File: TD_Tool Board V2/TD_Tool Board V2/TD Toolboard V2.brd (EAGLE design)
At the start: 54.2 x 49 mm, 140 parts, among them J3 JST-MICROFIT, M1 NMOSFET_WSD3066DN33, M2 CJ3400, M3 CJ3400, M4 CJ3400, P1 TPS54202_BUCKCONV, P2 3.3V, U1 RP2040, U2 W25Q128, U3 SN65HVD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

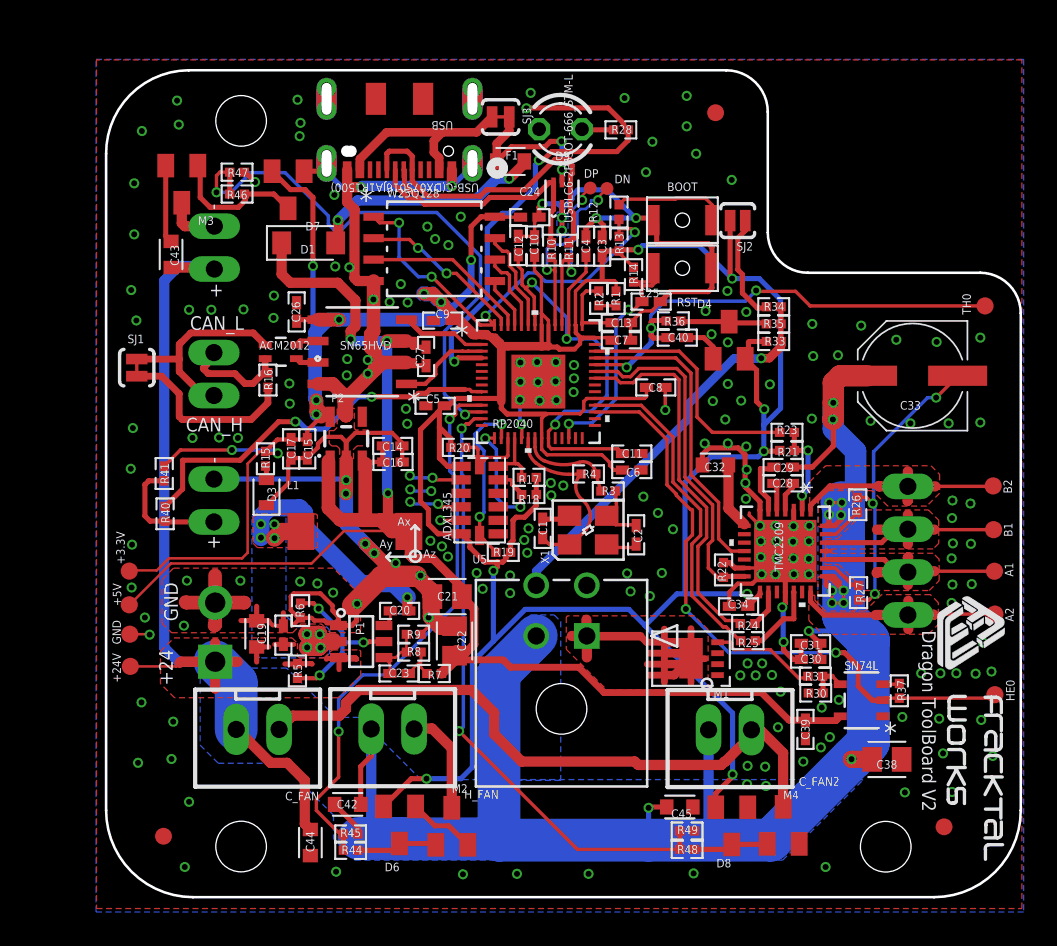
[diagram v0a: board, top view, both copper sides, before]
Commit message: minor changes in connector logic
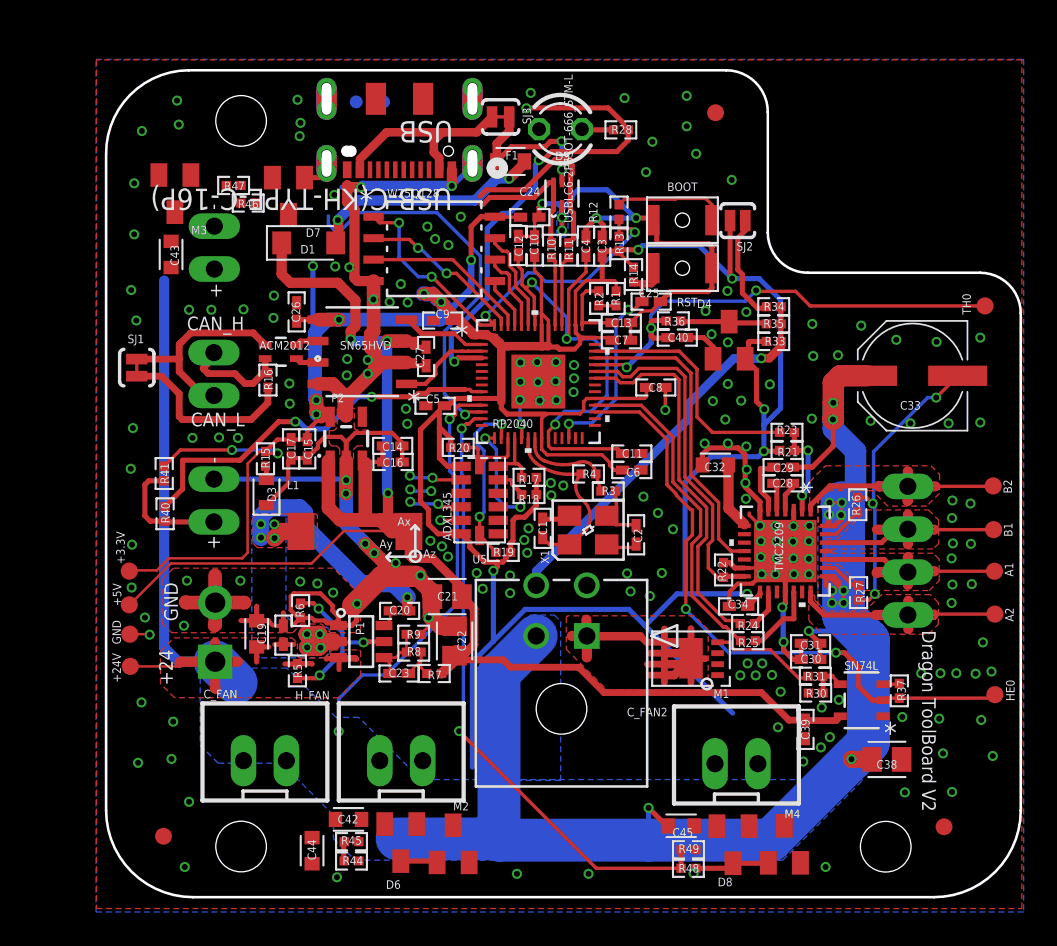
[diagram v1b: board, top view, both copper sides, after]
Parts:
- removed U$1: (no value), FracktalWorks_Eagle_Library:FWLOGO_SMALL
- USB: value USB-C(DX07S016JA1R1500) -> USB-C(KH-TYPE-C-16P); device CDC Library:CONN12_016JA1R1500_JAE -> Fracktal Misc Lib:CONN12_KH-TYPE-C-16P
- moved IO2 14.8 mm to (20.3, 52.1), flipped to the bottom
- moved IO1 14.2 mm to (21.9, 52.1), flipped to the bottom
- moved C_FAN2 2.04 mm to (42.8, 12.9), turned to 0 degrees
- moved H_FAN 1.95 mm to (23.0, 13.0), turned to 0 degrees
- moved C_FAN 1.90 mm to (14.9, 13.0), turned to 0 degrees
- moved C45 1.12 mm to (39.6, 9.17)
- moved M4 1.12 mm to (45.7, 8.08)
- moved R48 1.12 mm to (40.0, 6.65)
- moved D8 1.12 mm to (42.6, 8.05)
- moved R49 1.12 mm to (40.0, 7.75)
- moved D6 1.04 mm to (23.0, 8.18)
- moved M2 1.04 mm to (26.1, 8.10)
- moved C42 0.89 mm to (19.9, 9.55)
- moved R46 0.85 mm to (13.9, 46.1)
- moved R47 0.81 mm to (13.1, 47.1)
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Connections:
- removed net FAN1D: M3.3, M_FAN.1
- new net N$3: M3.3, M_FAN.2
- new net N$4: C_FAN.2, C_FAN2.2, M4.3
- net +24V: now also C_FAN.1, C_FAN2.1, H_FAN.1; no longer C_FAN.2, C_FAN2.2, H_FAN.2, M_FAN.2
- net N$1: now also H_FAN.2; no longer H_FAN.1
- net N$2: now also M_FAN.1; no longer C_FAN.1, C_FAN2.1, M4.3
- net USB1_N: now also IO1.P$1, USB.7; no longer USB.8
- net USB1_P: now also IO2.P$1, USB.8; no longer USB.7
- net USB_N: no longer IO1.P$1
- net USB_P: no longer IO2.P$1
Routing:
- net N$2: track 38.5 -> 0.00 mm
- net +24V: track 176.5 -> 138.1 mm
- net +3.3V: track 255.0 -> 235.7 mm, vias 17 -> 15
- net GND: track 215.3 -> 201.2 mm, vias 213 -> 207
- net FAN1: track 34.3 -> 23.0 mm, vias 2 -> 1
- net USB1_P: track 17.1 -> 8.50 mm
- net USB1_N: track 20.0 -> 11.5 mm
- net FAN1G: track 8.34 -> 0.00 mm
- net USB_N: track 11.4 -> 4.17 mm, vias 2 -> 0
- net FAN0: track 33.2 -> 26.0 mm
- net USB_P: track 11.0 -> 4.09 mm, vias 2 -> 0
- net N$1: track 6.25 -> 0.00 mm
- net FAN1D: track 3.22 -> 0.00 mm
- net FAN0G: track 4.81 -> 2.19 mm
- net VBUS: track 12.1 -> 11.4 mm
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
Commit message: routed the connections for the connectors whose logic were changed
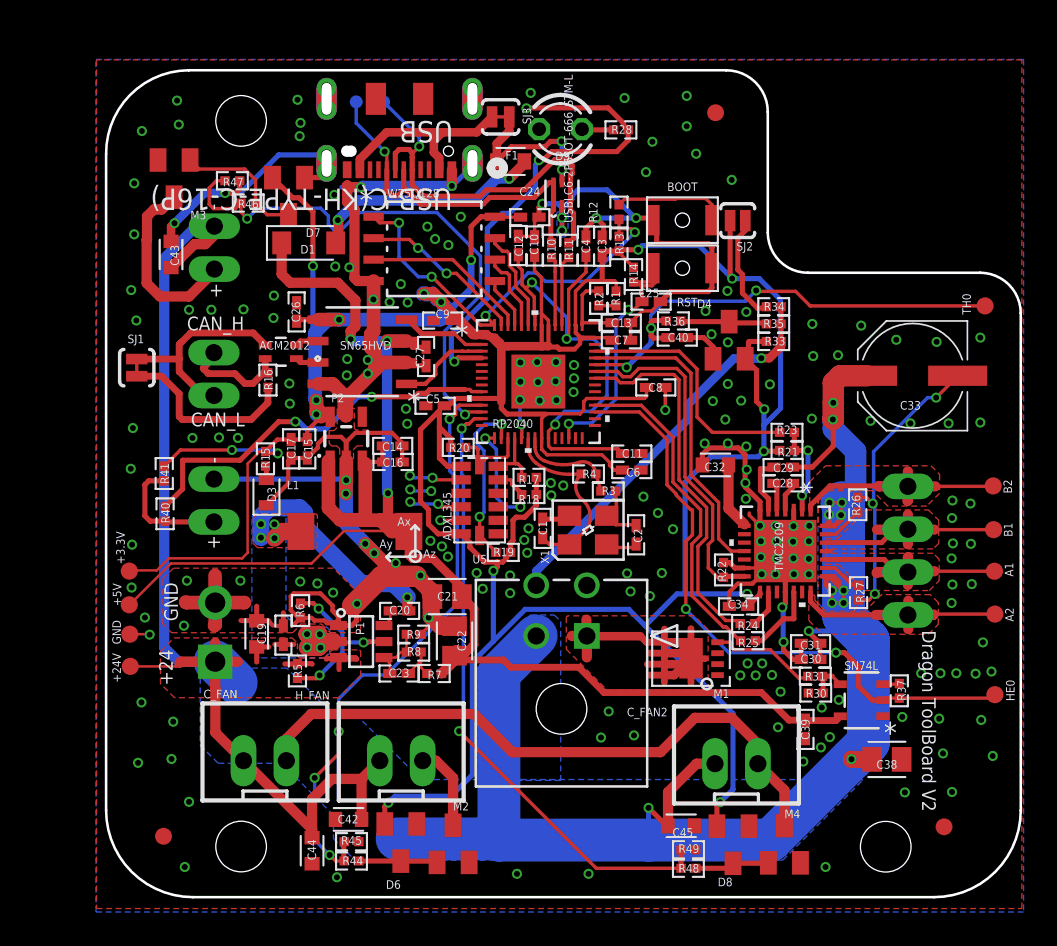
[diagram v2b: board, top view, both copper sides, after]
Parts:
- moved M3 0.89 mm to (9.53, 47.5)
- moved R47 0.29 mm to (13.0, 47.4)
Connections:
- removed net N$2: M_FAN.1
- net +24V: now also M_FAN.1
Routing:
- net N$4: track 0.00 -> 37.8 mm
- net +24V: track 138.1 -> 173.4 mm
- net +3.3V: track 235.7 -> 256.7 mm, vias 15 -> 17
- net USB1_P: track 8.50 -> 21.9 mm, vias 0 -> 1
- net GND: track 201.2 -> 214.5 mm, vias 207 -> 211
- net USB1_N: track 11.5 -> 24.1 mm, vias 0 -> 1
- net N$3: track 0.00 -> 11.1 mm
- net FAN1: track 23.0 -> 33.5 mm, vias 1 -> 2
- net FAN0: track 26.0 -> 35.3 mm, vias 2 -> 4
- net FAN1G: track 0.00 -> 7.98 mm
- net N$1: track 0.00 -> 5.04 mm
- net FAN0G: track 2.19 -> 4.67 mm
- net VBUS: track 11.4 -> 12.1 mm

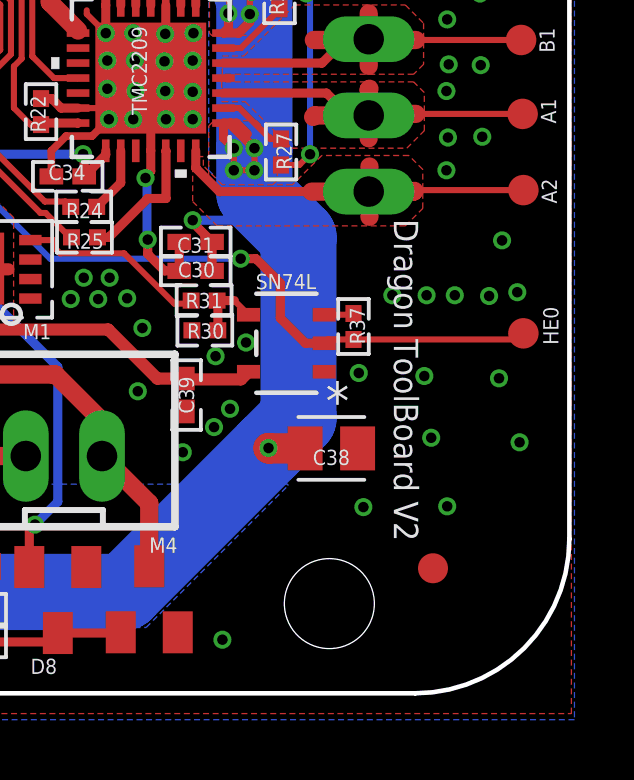
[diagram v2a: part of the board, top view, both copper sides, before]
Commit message: updated fracktal logo with bmp
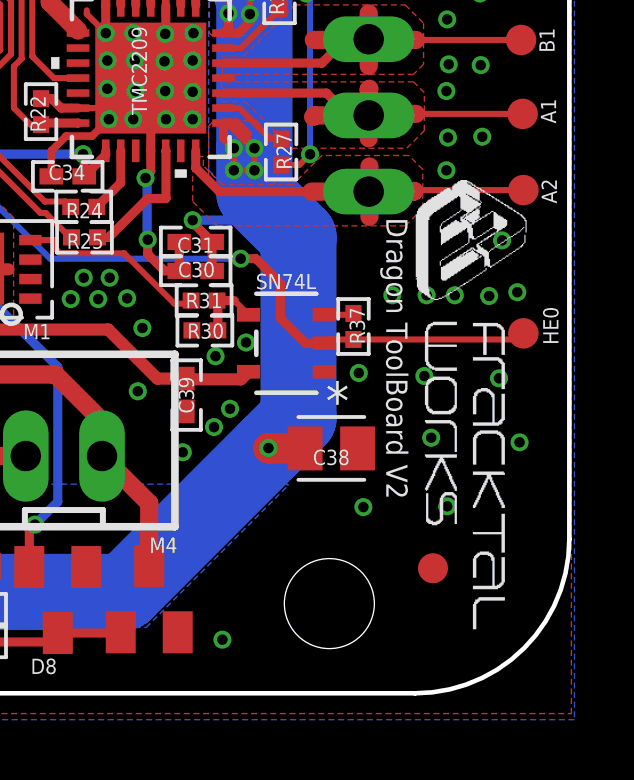
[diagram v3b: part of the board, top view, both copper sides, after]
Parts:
- added U$1: (no value), FracktalWorks_Eagle_Library:FRACKTAL_TNAMES_LOGO
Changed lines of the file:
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@@
 <text x="19.8628" y="53.1876" size="0.508" layer="26" font="vector" ratio="15" rot="MR180">DP</text>
 <text x="59.3344" y="16.5608" size="0.508" layer="25" font="vector" ratio="15" rot="R90">HE0</text>
-<text x="53.848" y="20.7518" size="0.8128" layer="25" rot="SR270">Dragon ToolBoard V2</text>
+<text x="53.594" y="20.8026" size="0.7112" layer="25" rot="SR270">Dragon ToolBoard V2</text>
 <text x="11.6078" y="40.5384" size="0.8128" layer="25" font="vector">+</text>
 <text x="12.2174" y="45.6692" size="0.8128" layer="25" font="vector" rot="R90">-</text>
@@
 <attribute name="VENDOR" value="LCSC" x="22.8854" y="49.149" size="0.508" layer="27" ratio="15" rot="R180" display="off"/>
 </element>
+<element name="U$1" library="FracktalWorks_Eagle_Library" package="FRACKTAL_TNAMES_LOGO" value="" x="52.7304" y="23.749" smashed="yes" rot="R270"/>
 </elements>
 <signals>

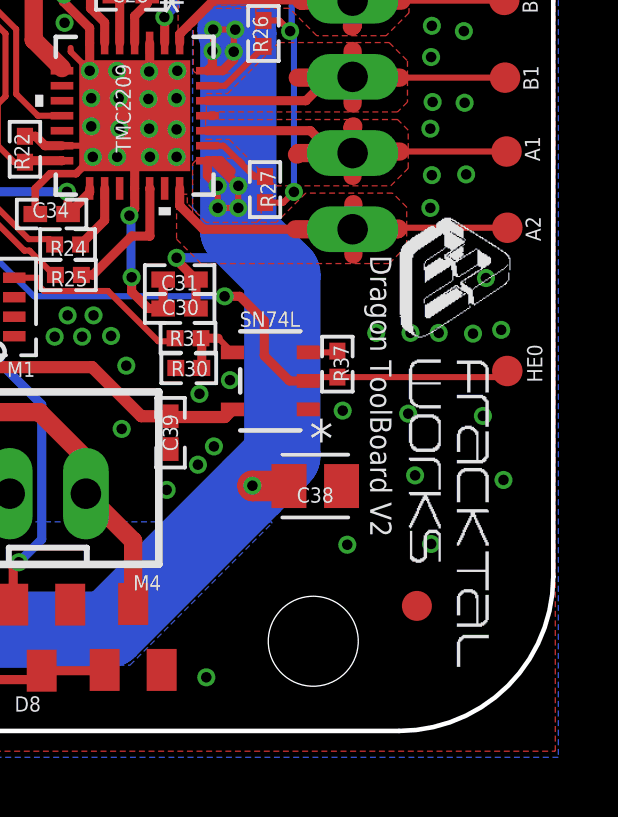
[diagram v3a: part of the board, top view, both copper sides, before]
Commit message: Logo, Centroid, BOM, datasheet changes and addition
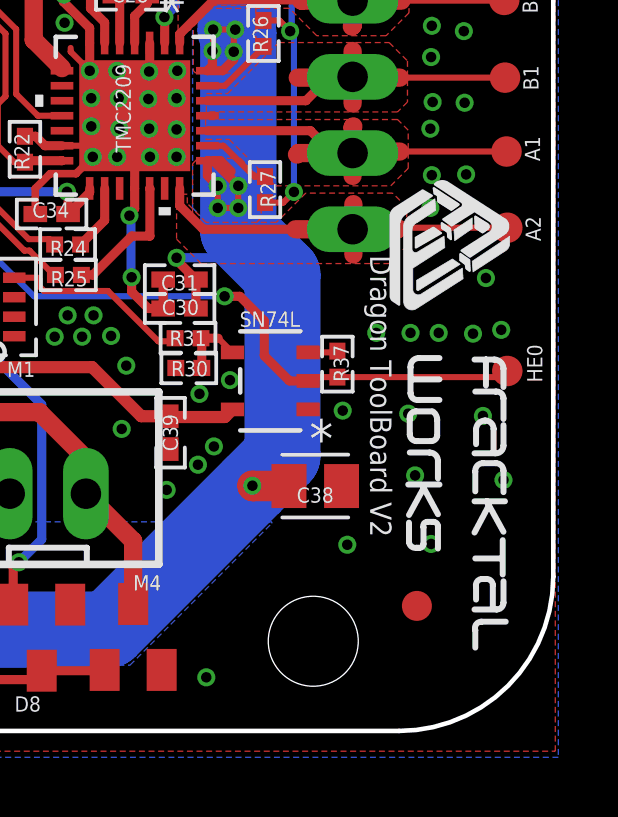
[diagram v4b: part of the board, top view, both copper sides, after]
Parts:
- removed U$1: (no value), FracktalWorks_Eagle_Library:FRACKTAL_TNAMES_LOGO
- added U$3: (no value), FracktalWorks_Eagle_Library:FWLOGO_SMALL
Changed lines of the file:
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@@
 <attribute name="VENDOR" value="LCSC" x="22.8854" y="49.149" size="0.508" layer="27" ratio="15" rot="R180" display="off"/>
 </element>
-<element name="U$1" library="FracktalWorks_Eagle_Library" package="FRACKTAL_TNAMES_LOGO" value="" x="52.7304" y="23.749" smashed="yes" rot="R270"/>
+<element name="U$3" library="FracktalWorks_Eagle_Library" package="FWLOGO_SMALL" value="" x="53.1114" y="23.5204" smashed="yes" rot="R270"/>
 </elements>
 <signals>

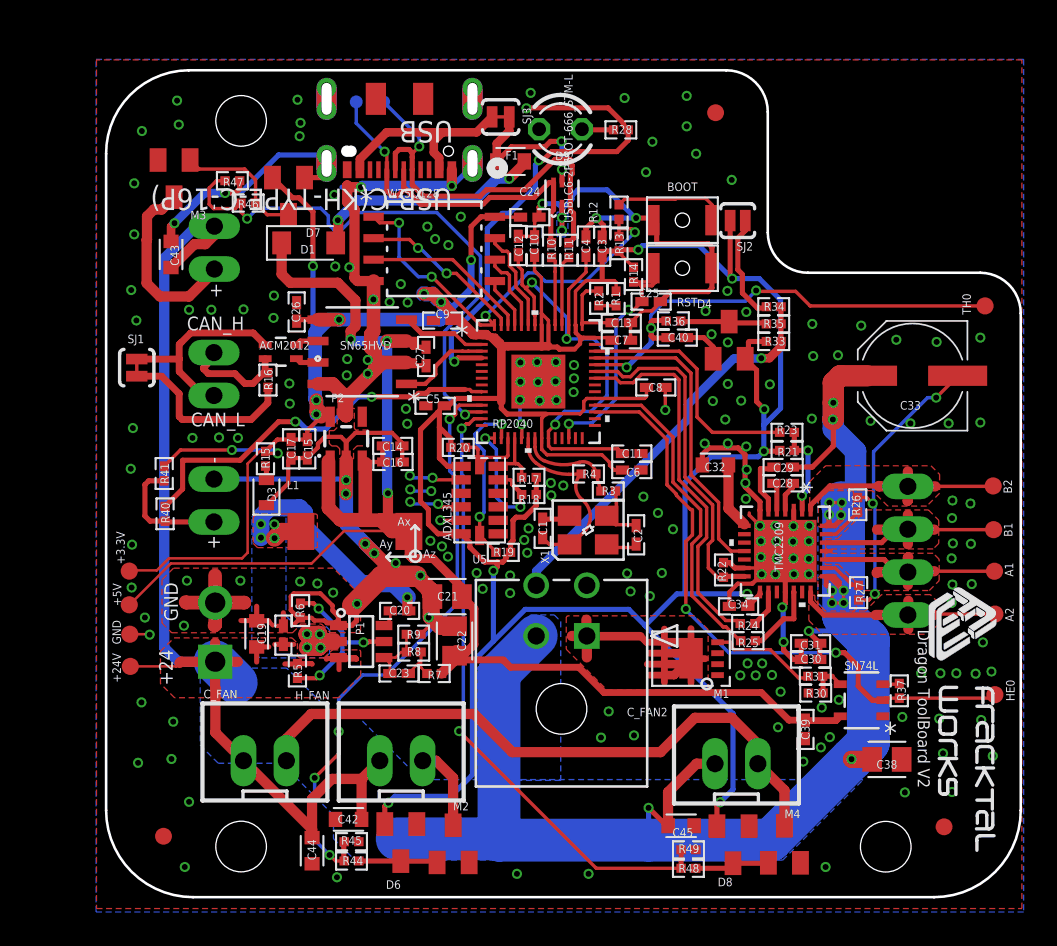
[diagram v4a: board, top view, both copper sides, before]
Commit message: Updated Toolboard V2 and Carriage minifit boards specs
Toolboard and Carriage minifit board design,  gerber, BOMs, centroids and connector specifications have been updated here
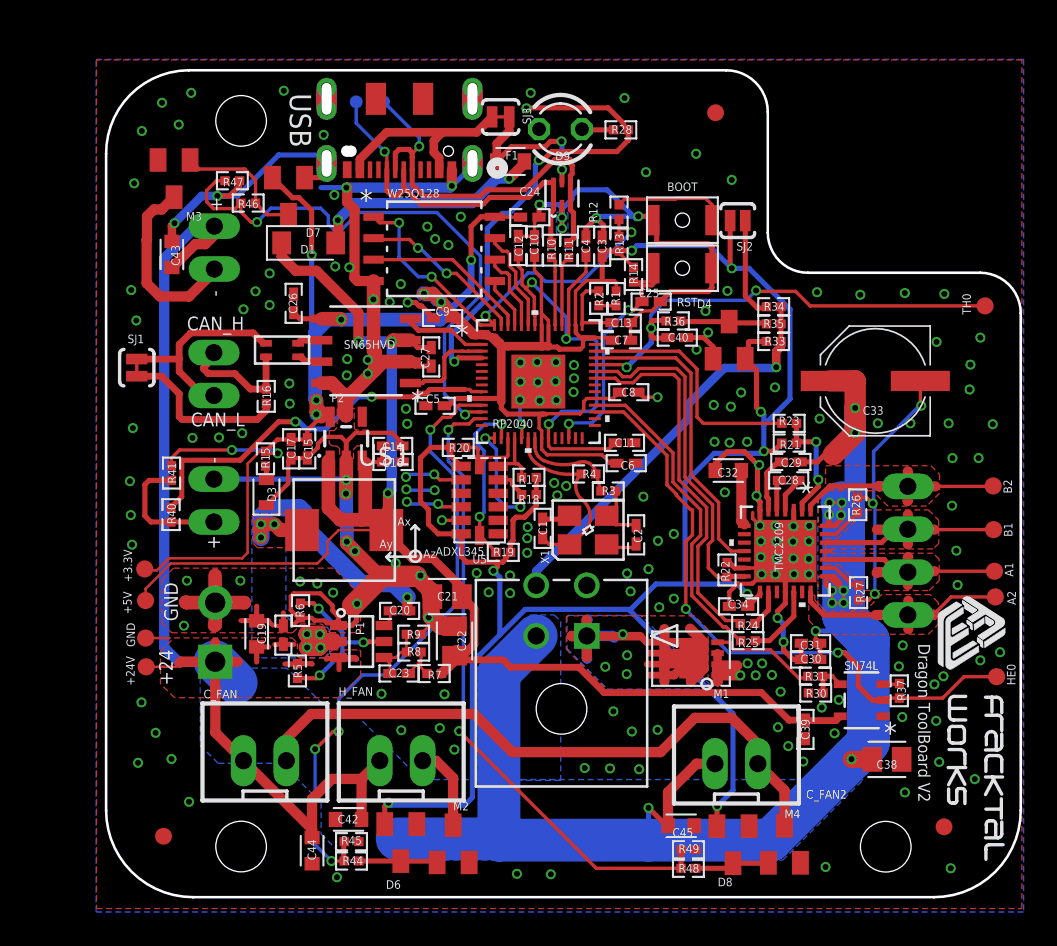
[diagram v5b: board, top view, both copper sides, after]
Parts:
- removed L1: ASPI-0630HI-100M-T157X7X4, Fracktal Misc Lib:SMDRI74-680MT
- removed L2: ACM2012, 2023-04-02_14-21-16_Library:ACM2012_TDK
- added U$1: YSPI0530-150, Fracktal_Dragon_ToolBoard_Components:YSPI0530-150
- added U$4: FDCW2012-2-201TF, Fracktal_Dragon_ToolBoard_Components:FDCW2012-2-201TF
- moved C33 2.23 mm to (51.1, 35.5)
- moved C8 1.62 mm to (36.5, 34.9)
- moved HE0 1.07 mm to (58.3, 18.0)
- moved A2 1.02 mm to (58.2, 22.7)
- moved 5V 1.00 mm to (7.84, 22.5)
- moved R16 0.97 mm to (15.0, 34.6)
- moved GND 0.97 mm to (7.84, 20.3)
- moved 24V 0.94 mm to (7.87, 18.6)
- moved 3.3V 0.92 mm to (7.79, 24.4)
- moved C32 0.83 mm to (42.4, 30.2)
- moved C11 0.77 mm to (36.2, 31.9)
- moved U$3 0.75 mm to (53.6, 23.0)
- moved C29 0.55 mm to (46.1, 30.7)
- moved R23 0.55 mm to (46.0, 33.0)
- moved C26 0.54 mm to (16.6, 40.1)
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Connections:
- net +5V: now also U$1.2; no longer L1.2
- net CAN1_N: now also U$4.2; no longer L2.2
- net CAN1_P: now also U$4.1; no longer L2.1
- net CAN_N: now also U$4.3; no longer L2.3
- net CAN_P: now also U$4.4; no longer L2.4
- net VREGO: now also U$1.1; no longer L1.1
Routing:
- net HE0_PWR: track 25.7 -> 34.5 mm, vias 0 -> 4
- net +3.3V: track 256.7 -> 249.7 mm
- net GND: track 214.5 -> 221.2 mm, vias 211 -> 203
- net +5V: track 97.3 -> 91.1 mm
- net VREGO: track 20.2 -> 21.8 mm, vias 9 -> 8
- net FAN0: track 35.3 -> 36.8 mm
- net TMCENN: track 5.58 -> 6.94 mm
- net FAN2: track 37.1 -> 38.2 mm
- net CNT: track 10.9 -> 10.1 mm
- net CAN_P: track 6.55 -> 7.33 mm
- net +1.1V: track 29.9 -> 29.1 mm
- net +24V: track 173.4 -> 174.0 mm
- net TMC5V: track 4.00 -> 3.35 mm
- net TH0A: track 23.7 -> 24.3 mm
- net E0_DIR: track 19.7 -> 19.2 mm
- added copper zone on layer 16, net HE0_PWR
